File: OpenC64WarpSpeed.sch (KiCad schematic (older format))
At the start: 18 parts, among them P1 C64-Exp-Port, SW1 SW_C64_C128, SW2 SW_RESET, SW3 SW_ROM, U1 74LS109, U2 27512

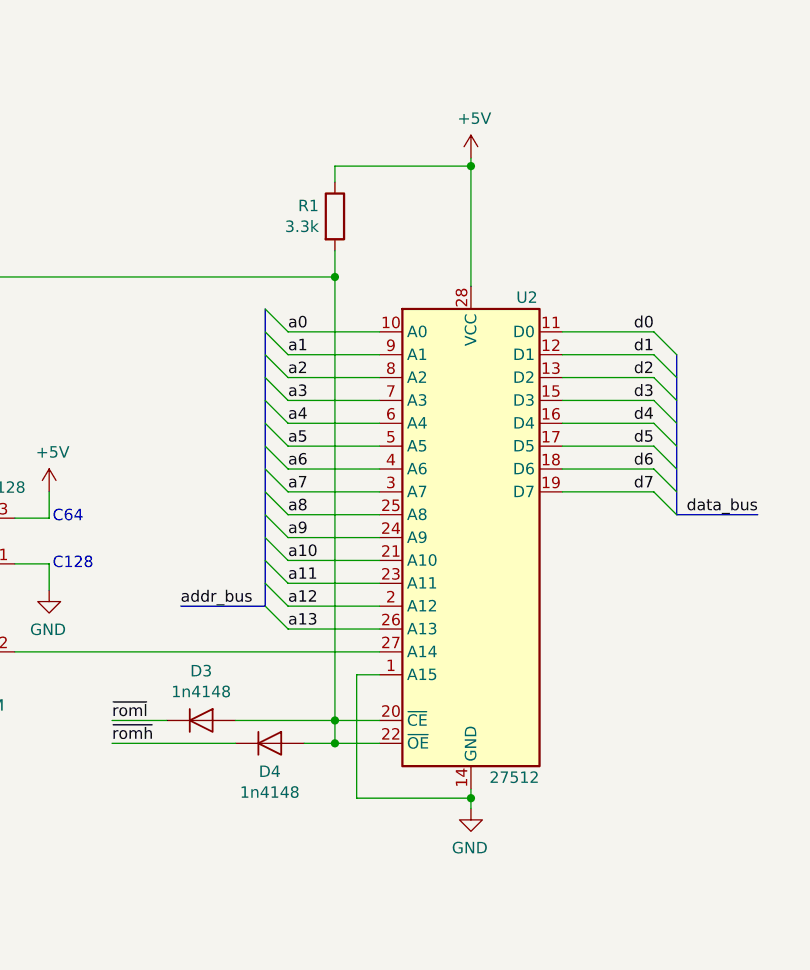
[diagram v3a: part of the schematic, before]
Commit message: Switch to a 27256 EPROM, but a 27512 can still be used (use upper 32K)
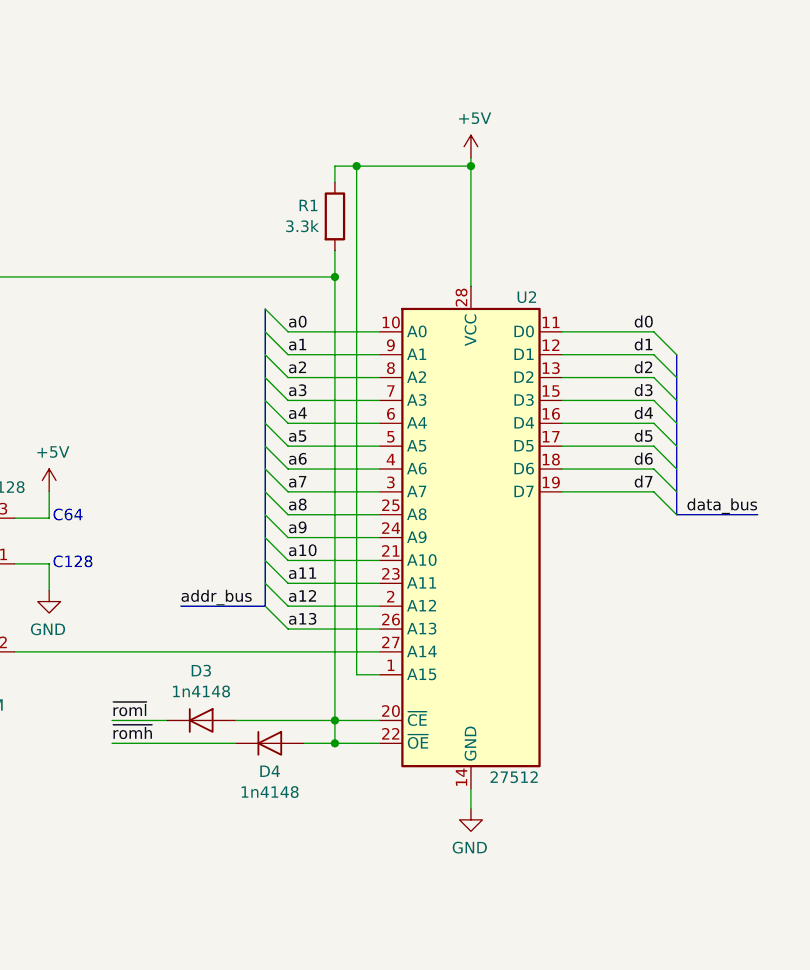
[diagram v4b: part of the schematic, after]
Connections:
- net +5V: now also U2.1 (A15)
- net GND: no longer U2.1 (A15)
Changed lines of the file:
@@
-$EndComp
-$Comp
-L Switch:SW_Push SW2
-U 1 1 5F59F12C
-P 4660 2835
-F 0 "SW2" H 4660 3120 50  0000 C CNN
-F 1 "SW_RESET" H 4660 3029 50  0000 C CNN
-F 2 "Button_Switch_THT:SW_PUSH_6mm" H 4660 3035 50  0001 C CNN
-F 3 "~" H 4660 3035 50  0001 C CNN
-	1    4660 2835
-	1    0    0    -1
 $EndComp
 $Comp
@@
 	2120 3075 2120 2330
 Wire Wire Line
-	2120 2330 4350 2330
-Wire Wire Line
-	4350 2330 4350 2835
-Wire Wire Line
-	4350 2835 4460 2835
-Wire Wire Line
-	4860 2835 4950 2835
-Wire Wire Line
-	4950 2835 4950 2900
-$Comp
-L power:GND #PWR0104
-U 1 1 5F5A976B
-P 4950 2900
-F 0 "#PWR0104" H 4950 2650 50  0001 C CNN
-F 1 "GND" H 4955 2727 50  0000 C CNN
-F 2 "" H 4950 2900 50  0001 C CNN
-F 3 "" H 4950 2900 50  0001 C CNN
-	1    4950 2900
-	-1   0    0    -1
-$EndComp
-Wire Wire Line
-	4350 2835 4350 3205
-Wire Wire Line
-	4350 3205 5755 3205
-Wire Wire Line
 	5755 3205 5755 3260
-Connection ~ 4350 2835
 $Comp
 L power:+5V #PWR0105
@@
 	-1   0    0    -1
 $EndComp
-Wire Wire Line
-	8890 5095 8890 5050
 Wire Wire Line
 	8490 4710 8295 4710
@@
 $EndComp
 Wire Wire Line
-	8295 2285 8890 2285
+	8295 2285 8390 2285
 Wire Wire Line
 	8490 4510 8390 4510
-Wire Wire Line
-	8390 4510 8390 5050
-Wire Wire Line
-	8390 5050 8890 5050
-Connection ~ 8890 5050
-Wire Wire Line
-	8890 5050 8890 5010
 $Comp
 L Switch:SW_DPDT_x2 SW3
@@
 NoConn ~ 4670 7120
 NoConn ~ 4270 7020
+$Comp
+L power:GND #PWR0104
+U 1 1 5F5A976B
+P 4950 2900
+F 0 "#PWR0104" H 4950 2650 50  0001 C CNN
+F 1 "GND" H 4955 2727 50  0000 C CNN
+F 2 "" H 4950 2900 50  0001 C CNN
+F 3 "" H 4950 2900 50  0001 C CNN
+	1    4950 2900
+	-1   0    0    -1
+$EndComp
+Wire Wire Line
+	4950 2835 4950 2900
+Wire Wire Line
+	4860 2835 4950 2835
+$Comp
+L Switch:SW_Push SW2
+U 1 1 5F59F12C
+P 4660 2835
+F 0 "SW2" H 4660 3120 50  0000 C CNN
+F 1 "SW_RESET" H 4660 3029 50  0000 C CNN
+F 2 "Button_Switch_THT:SW_PUSH_6mm" H 4660 3035 50  0001 C CNN
+F 3 "~" H 4660 3035 50  0001 C CNN
+	1    4660 2835
+	1    0    0    -1
+$EndComp
+Connection ~ 4350 2835
+Wire Wire Line
+	4350 3205 5755 3205
+Wire Wire Line
+	4350 2835 4350 3205
+Wire Wire Line
+	4350 2835 4460 2835
+Wire Wire Line
+	4350 2330 4350 2835
+Wire Wire Line
+	2120 2330 4350 2330
+Wire Wire Line
+	8390 4510 8390 2285
+Connection ~ 8390 2285
+Wire Wire Line
+	8390 2285 8890 2285
+Wire Wire Line
+	8890 5010 8890 5095
 Wire Bus Line
 	4345 4275 4345 4975
